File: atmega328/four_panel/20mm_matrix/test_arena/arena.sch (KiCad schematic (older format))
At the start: 29 parts, among them P1 CONN15, P10 CONN_2X2, P11 CONN_2X2, P12 CONN_2X2, P13 CONN_2X2, P14 CONN_2X2, P15 CONN_2X2, P16 CONN_2X2, P17 CONN_2X2, P18 CONN_2X2, P19 CONN_2X2, P2 CONN15, P20 CONN_2X2, P21 CONN_2X2, P22 CONN_20X2, P23 CONN_30X2, P24 CONN_2, P3 CONN15, P4 CONN15, P5 CONN15, P6 CONN15, P7 CONN_2X2, P8 CONN_2X2, P9 CONN_2X2

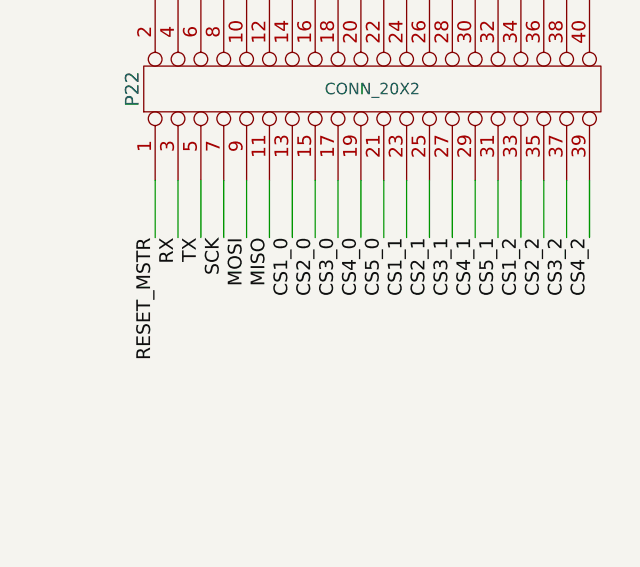
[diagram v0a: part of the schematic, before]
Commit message: Finished test arena for 4 x 20mm atmega328 panels.
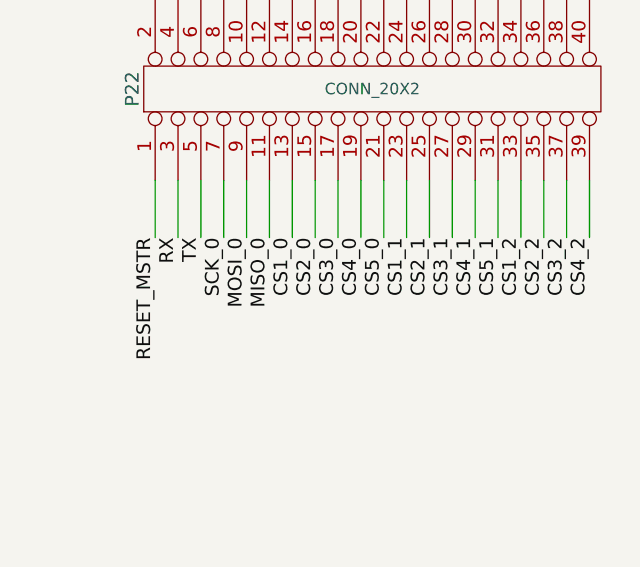
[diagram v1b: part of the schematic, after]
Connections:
- net MISO is gone; now on net MISO_0: P22.11 (P11)
- net MOSI is gone; now on net MOSI_0: P22.9 (P9)
- net SCK is gone; now on net SCK_0: P22.7 (P7)
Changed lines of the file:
@@
 LIBS:valves
 LIBS:conn15
+LIBS:arena-cache
 EELAYER 24 0
 EELAYER END
@@
 	2150 9700 2150 9850
 $Comp
-L +5V #PWR19
+L +5V #PWR01
 U 1 1 524B46C2
 P 2150 9300
-F 0 "#PWR19" H 2150 9390 20  0001 C CNN
+F 0 "#PWR01" H 2150 9390 20  0001 C CNN
 F 1 "+5V" H 2150 9390 30  0000 C CNN
 F 2 "" H 2150 9300 60  0000 C CNN
@@
 $EndComp
 $Comp
-L GND #PWR21
+L GND #PWR02
 U 1 1 524B46D1
 P 2150 9850
-F 0 "#PWR21" H 2150 9850 30  0001 C CNN
+F 0 "#PWR02" H 2150 9850 30  0001 C CNN
 F 1 "GND" H 2150 9780 30  0001 C CNN
 F 2 "" H 2150 9850 60  0000 C CNN
@@
 $EndComp
 $Comp
-L PWR_FLAG #FLG1
+L PWR_FLAG #FLG03
 U 1 1 524B46EA
 P 1250 9400
-F 0 "#FLG1" H 1250 9495 30  0001 C CNN
+F 0 "#FLG03" H 1250 9495 30  0001 C CNN
 F 1 "PWR_FLAG" H 1250 9580 30  0000 C CNN
 F 2 "" H 1250 9400 60  0000 C CNN
@@
 $EndComp
 $Comp
-L PWR_FLAG #FLG2
+L PWR_FLAG #FLG04
 U 1 1 524B46F9
 P 1650 9400
-F 0 "#FLG2" H 1650 9495 30  0001 C CNN
+F 0 "#FLG04" H 1650 9495 30  0001 C CNN
 F 1 "PWR_FLAG" H 1650 9580 30  0000 C CNN
 F 2 "" H 1650 9400 60  0000 C CNN
@@
 	1650 9400 1650 9850
 $Comp
-L GND #PWR20
+L GND #PWR05
 U 1 1 524B471D
 P 1650 9850
-F 0 "#PWR20" H 1650 9850 30  0001 C CNN
+F 0 "#PWR05" H 1650 9850 30  0001 C CNN
 F 1 "GND" H 1650 9780 30  0001 C CNN
 F 2 "" H 1650 9850 60  0000 C CNN
@@
 	900  9550 900  9300
 $Comp
-L +5V #PWR18
+L +5V #PWR06
 U 1 1 524B473D
 P 900 9300
-F 0 "#PWR18" H 900 9390 20  0001 C CNN
+F 0 "#PWR06" H 900 9390 20  0001 C CNN
 F 1 "+5V" H 900 9390 30  0000 C CNN
 F 2 "" H 900 9300 60  0000 C CNN
@@
 	850  1000 850  1200
 $Comp
-L +5V #PWR1
+L +5V #PWR07
 U 1 1 524B47C6
 P 850 1000
-F 0 "#PWR1" H 850 1090 20  0001 C CNN
+F 0 "#PWR07" H 850 1090 20  0001 C CNN
 F 1 "+5V" H 850 1090 30  0000 C CNN
 F 2 "" H 850 1000 60  0000 C CNN
@@
 	850  1300 850  1450
 $Comp
-L GND #PWR7
+L GND #PWR08
 U 1 1 524B47EA
 P 850 1450
-F 0 "#PWR7" H 850 1450 30  0001 C CNN
+F 0 "#PWR08" H 850 1450 30  0001 C CNN
 F 1 "GND" H 850 1380 30  0001 C CNN
 F 2 "" H 850 1450 60  0000 C CNN
@@
 	2600 1000 2600 1200
 $Comp
-L +5V #PWR2
+L +5V #PWR09
 U 1 1 524B4A08
 P 2600 1000
-F 0 "#PWR2" H 2600 1090 20  0001 C CNN
+F 0 "#PWR09" H 2600 1090 20  0001 C CNN
 F 1 "+5V" H 2600 1090 30  0000 C CNN
 F 2 "" H 2600 1000 60  0000 C CNN
@@
 	2600 1300 2600 1450
 $Comp
-L GND #PWR8
+L GND #PWR010
 U 1 1 524B4A10
 P 2600 1450
-F 0 "#PWR8" H 2600 1450 30  0001 C CNN
+F 0 "#PWR010" H 2600 1450 30  0001 C CNN
 F 1 "GND" H 2600 1380 30  0001 C CNN
 F 2 "" H 2600 1450 60  0000 C CNN
@@
 	4350 1000 4350 1200
 $Comp
-L +5V #PWR3
+L +5V #PWR011
 U 1 1 524B4A63
 P 4350 1000
-F 0 "#PWR3" H 4350 1090 20  0001 C CNN
+F 0 "#PWR011" H 4350 1090 20  0001 C CNN
 F 1 "+5V" H 4350 1090 30  0000 C CNN
 F 2 "" H 4350 1000 60  0000 C CNN
@@
 	4350 1300 4350 1450
 $Comp
-L GND #PWR9
+L GND #PWR012
 U 1 1 524B4A6B
 P 4350 1450
-F 0 "#PWR9" H 4350 1450 30  0001 C CNN
+F 0 "#PWR012" H 4350 1450 30  0001 C CNN
 F 1 "GND" H 4350 1380 30  0001 C CNN
 F 2 "" H 4350 1450 60  0000 C CNN
@@
 	6100 1000 6100 1200
 $Comp
-L +5V #PWR4
+L +5V #PWR013
 U 1 1 524B4A94
 P 6100 1000
-F 0 "#PWR4" H 6100 1090 20  0001 C CNN
+F 0 "#PWR013" H 6100 1090 20  0001 C CNN
 F 1 "+5V" H 6100 1090 30  0000 C CNN
 F 2 "" H 6100 1000 60  0000 C CNN
@@
 	6100 1300 6100 1450
 $Comp
-L GND #PWR10
+L GND #PWR014
 U 1 1 524B4A9C
 P 6100 1450
-F 0 "#PWR10" H 6100 1450 30  0001 C CNN
+F 0 "#PWR014" H 6100 1450 30  0001 C CNN
 F 1 "GND" H 6100 1380 30  0001 C CNN
 F 2 "" H 6100 1450 60  0000 C CNN
@@
 	7800 1000 7800 1200
 $Comp
-L +5V #PWR5
+L +5V #PWR015
 U 1 1 524B4AC7
 P 7800 1000
-F 0 "#PWR5" H 7800 1090 20  0001 C CNN
+F 0 "#PWR015" H 7800 1090 20  0001 C CNN
 F 1 "+5V" H 7800 1090 30  0000 C CNN
 F 2 "" H 7800 1000 60  0000 C CNN
@@
 	7800 1300 7800 1450
 $Comp
-L GND #PWR11
+L GND #PWR016
 U 1 1 524B4ACF
 P 7800 1450
-F 0 "#PWR11" H 7800 1450 30  0001 C CNN
+F 0 "#PWR016" H 7800 1450 30  0001 C CNN
 F 1 "GND" H 7800 1380 30  0001 C CNN
 F 2 "" H 7800 1450 60  0000 C CNN
@@
 	9450 1000 9450 1200
 $Comp
-L +5V #PWR6
+L +5V #PWR017
 U 1 1 524B5E35
 P 9450 1000
-F 0 "#PWR6" H 9450 1090 20  0001 C CNN
+F 0 "#PWR017" H 9450 1090 20  0001 C CNN
 F 1 "+5V" H 9450 1090 30  0000 C CNN
 F 2 "" H 9450 1000 60  0000 C CNN
@@
 	9450 1300 9450 1450
 $Comp
-L GND #PWR12
+L GND #PWR018
 U 1 1 524B5E3D
 P 9450 1450
-F 0 "#PWR12" H 9450 1450 30  0001 C CNN
+F 0 "#PWR018" H 9450 1450 30  0001 C CNN
 F 1 "GND" H 9450 1380 30  0001 C CNN
 F 2 "" H 9450 1450 60  0000 C CNN
@@
 Connection ~ 8500 7400
 $Comp
-L +5V #PWR14
+L +5V #PWR019
 U 1 1 524B6E04
 P 8500 5850
-F 0 "#PWR14" H 8500 5940 20  0001 C CNN
+F 0 "#PWR019" H 8500 5940 20  0001 C CNN
 F 1 "+5V" H 8500 5940 30  0000 C CNN
 F 2 "" H 8500 5850 60  0000 C CNN
@@
 $EndComp
 $Comp
-L GND #PWR16
+L GND #PWR020
 U 1 1 524B6E13
 P 8500 7650
-F 0 "#PWR16" H 8500 7650 30  0001 C CNN
+F 0 "#PWR020" H 8500 7650 30  0001 C CNN
 F 1 "GND" H 8500 7580 30  0001 C CNN
 F 2 "" H 8500 7650 60  0000 C CNN
@@
 	1550 7100 1550 7350
 Text Label 1350 7350 3    60   ~ 0
-SCK
+SCK_0
 Text Label 1450 7350 3    60   ~ 0
-MOSI
+MOSI_0
 Text Label 1550 7350 3    60   ~ 0
-MISO
+MISO_0
 Wire Wire Line
 	1650 7100 1650 7350
@@
 	3250 6150 3250 6350
 $Comp
-L +5V #PWR13
+L +5V #PWR021
 U 1 1 524B710E
 P 2850 5800
-F 0 "#PWR13" H 2850 5890 20  0001 C CNN
+F 0 "#PWR021" H 2850 5890 20  0001 C CNN
 F 1 "+5V" H 2850 5890 30  0000 C CNN
 F 2 "" H 2850 5800 60  0000 C CNN
@@
 $EndComp
 $Comp
-L GND #PWR15
+L GND #PWR022
 U 1 1 524B711D
 P 3250 6350
-F 0 "#PWR15" H 3250 6350 30  0001 C CNN
+F 0 "#PWR022" H 3250 6350 30  0001 C CNN
 F 1 "GND" H 3250 6280 30  0001 C CNN
 F 2 "" H 3250 6350 60  0000 C CNN
@@
 $EndComp
 $Comp
-L +5V #PWR17
+L +5V #PWR023
 U 1 1 524BBCA1
 P 5000 8950
-F 0 "#PWR17" H 5000 9040 20  0001 C CNN
+F 0 "#PWR023" H 5000 9040 20  0001 C CNN
 F 1 "+5V" H 5000 9040 30  0000 C CNN
 F 2 "" H 5000 8950 60  0000 C CNN
@@
 $EndComp
 $Comp
-L GND #PWR22
+L GND #PWR024
 U 1 1 524BBCDD
 P 5000 10150
-F 0 "#PWR22" H 5000 10150 30  0001 C CNN
+F 0 "#PWR024" H 5000 10150 30  0001 C CNN
 F 1 "GND" H 5000 10080 30  0001 C CNN
 F 2 "" H 5000 10150 60  0000 C CNN

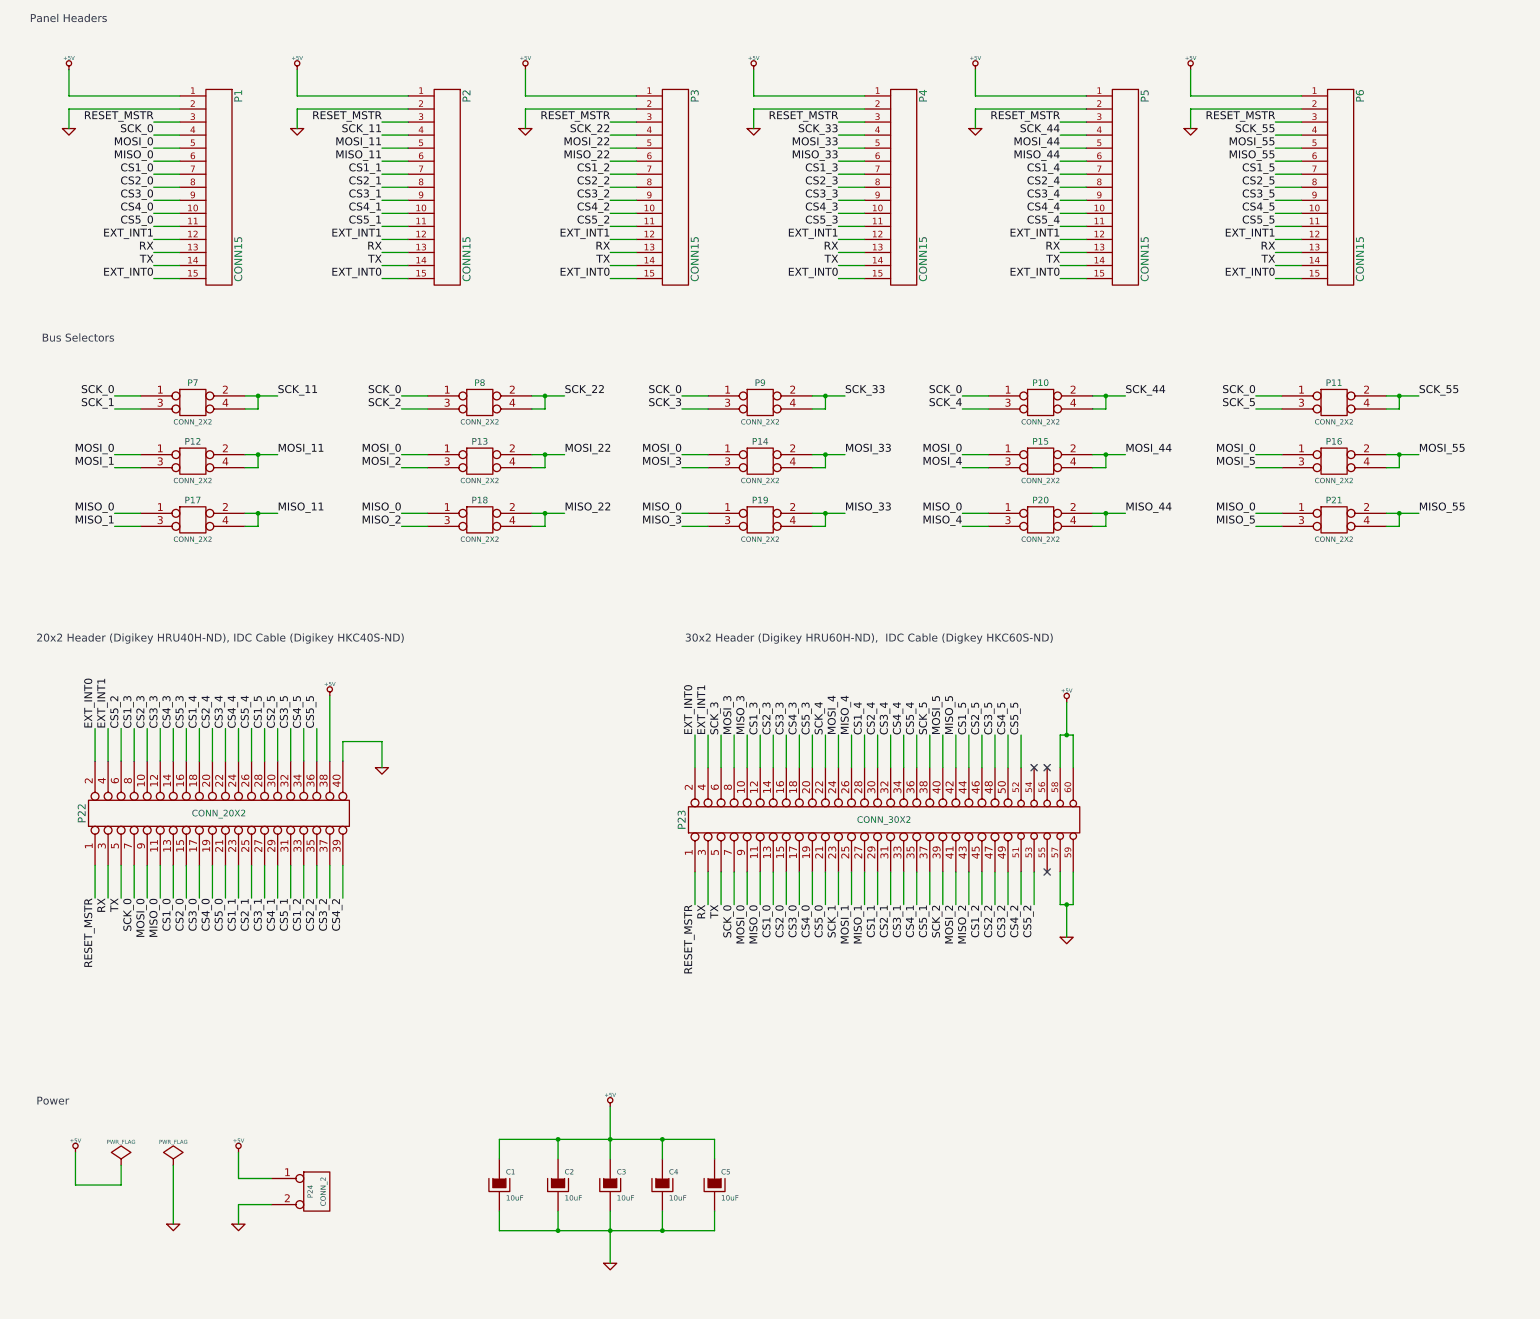
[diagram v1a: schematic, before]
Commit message: Finished 4x20mm matrix MAX6960 test arena.
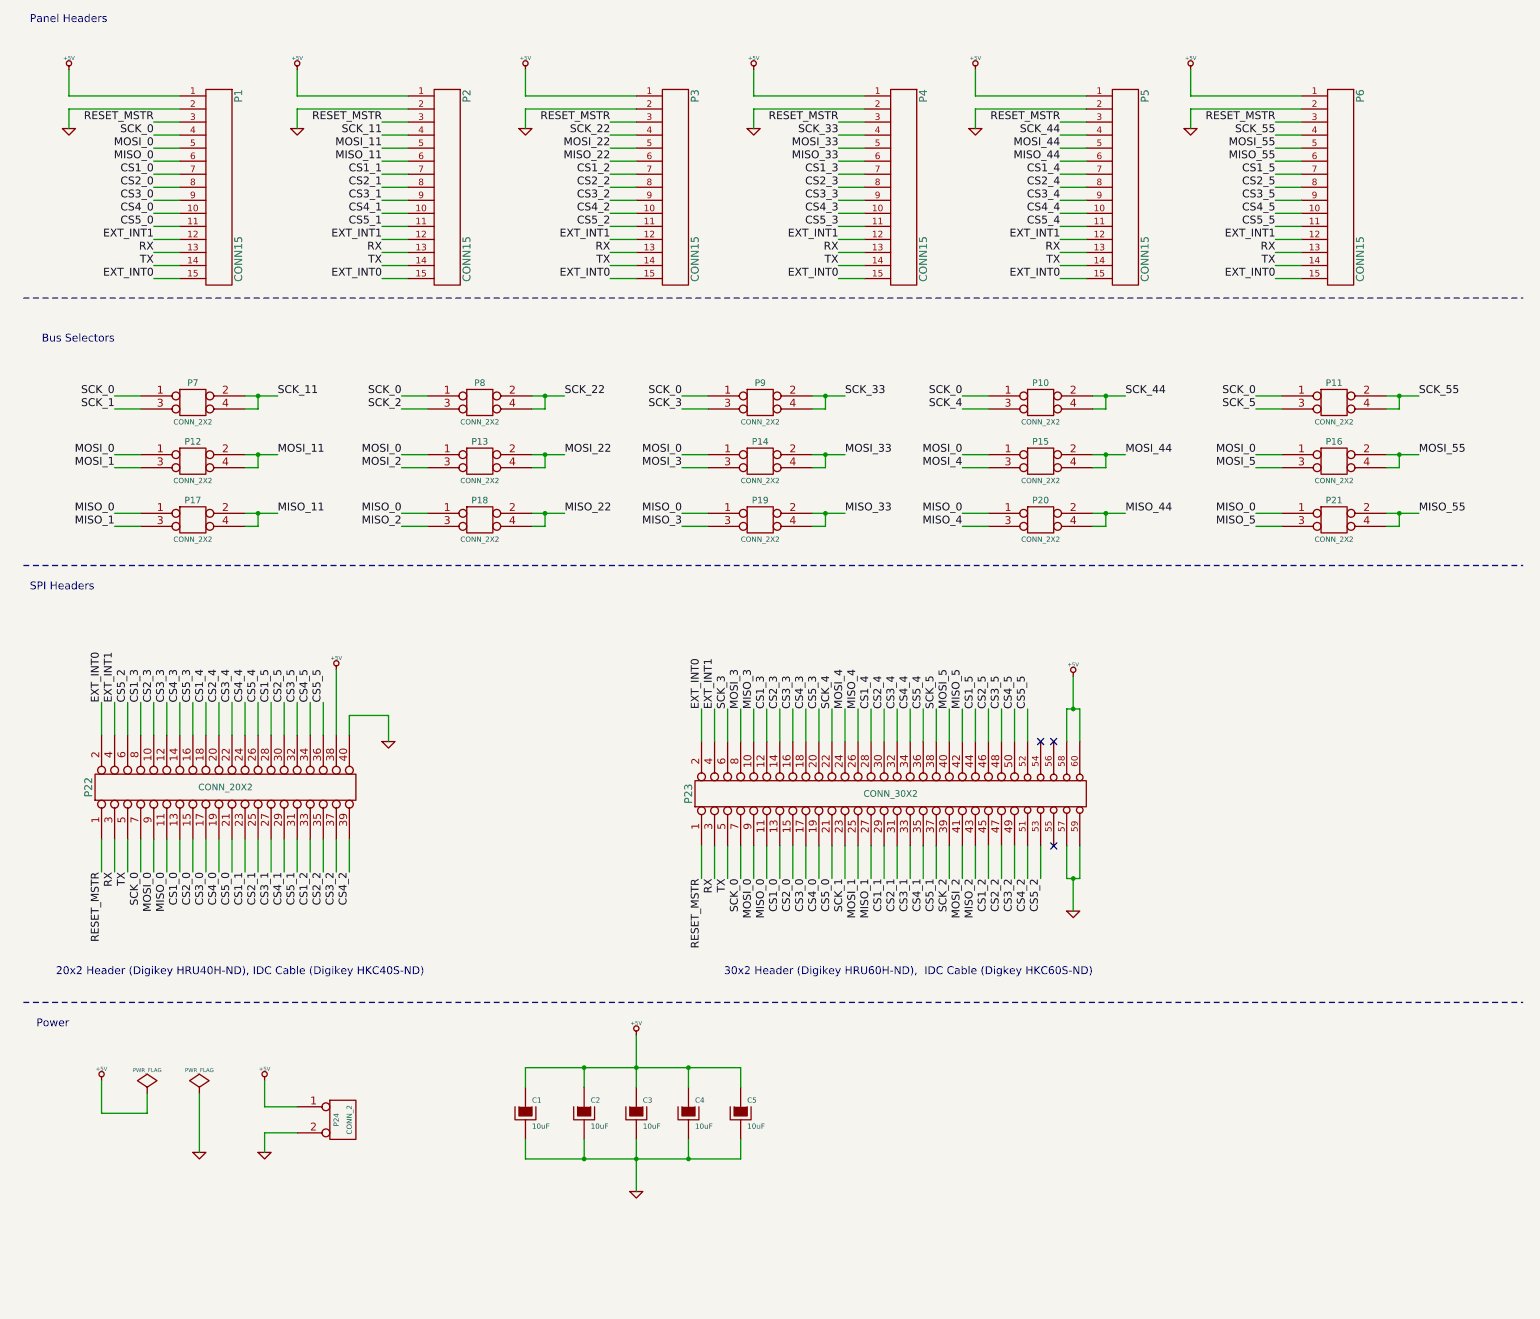
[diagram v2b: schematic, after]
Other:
- note added: "SPI Headers"
- moved on the sheet: C1, C2, C3, C4, C5, P22, P23, P24

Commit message: Added second communications header w/ common CS lines to  atmega328 4x20mm  test arena.
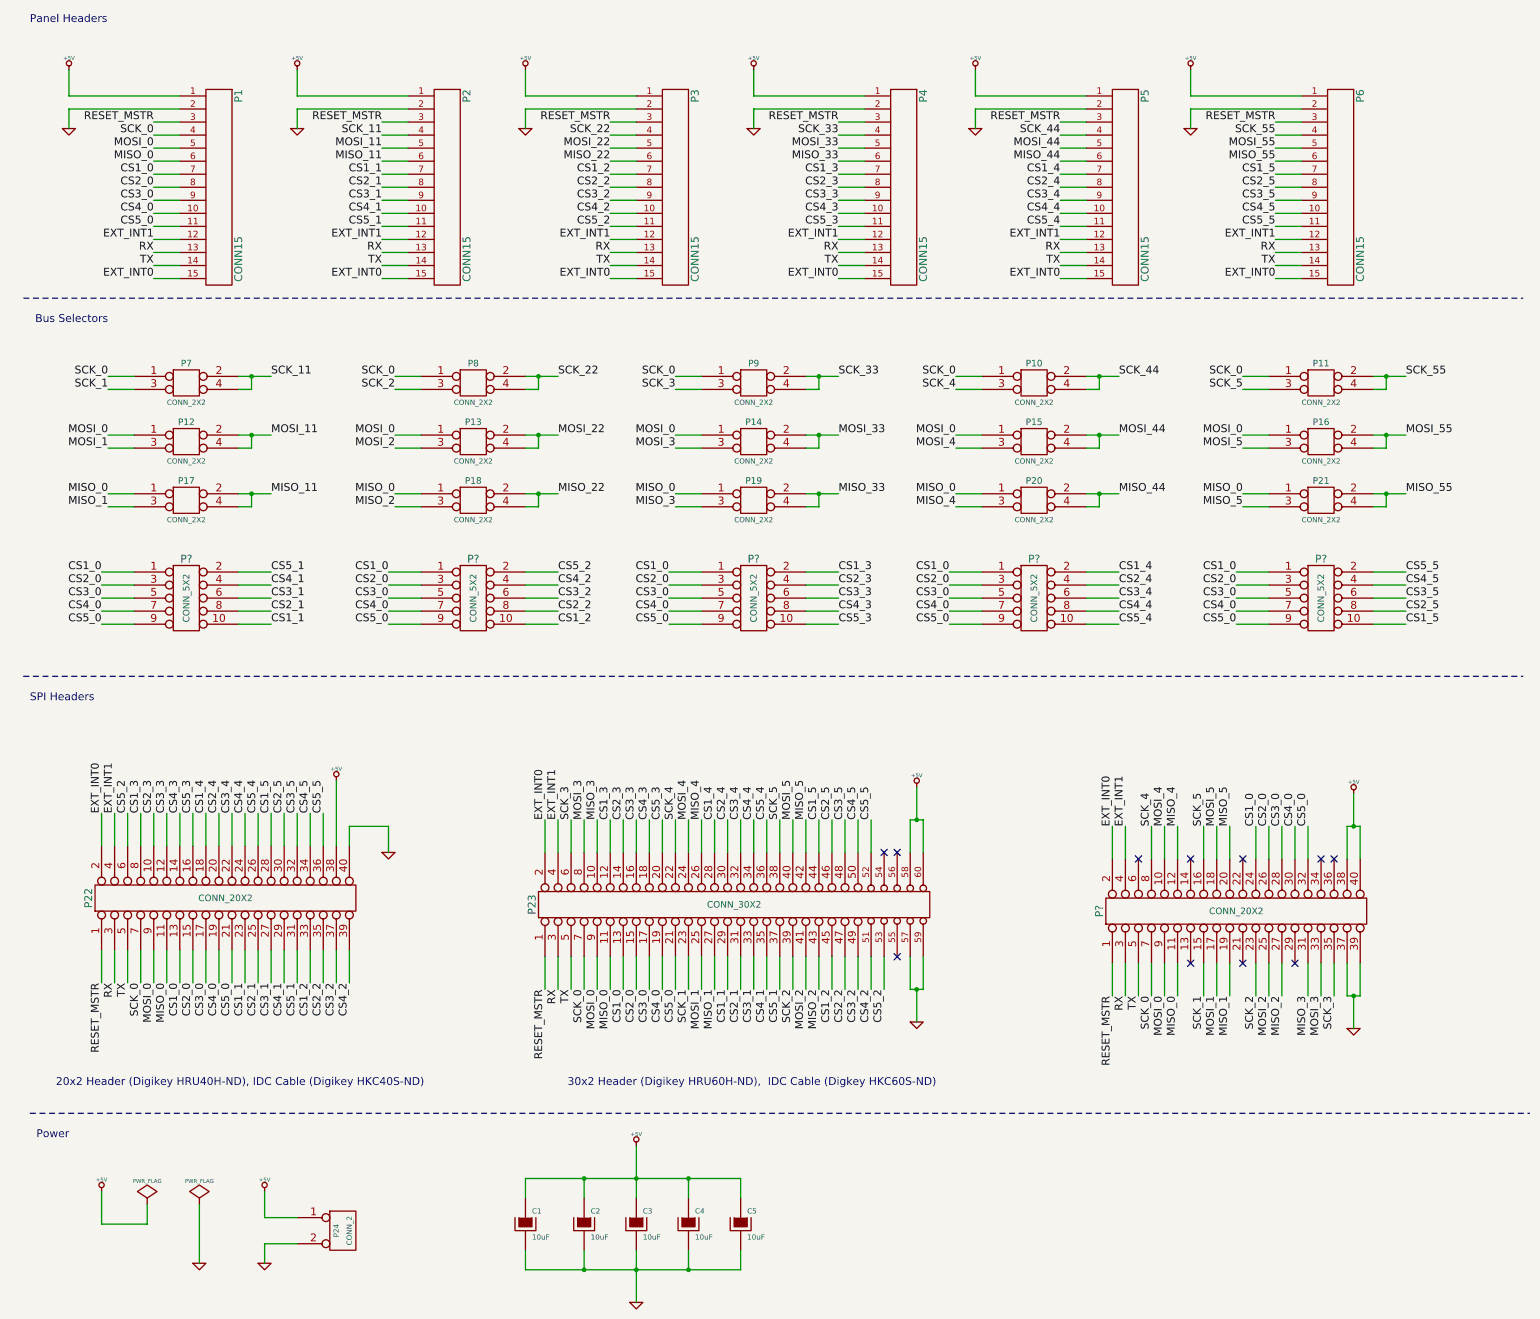
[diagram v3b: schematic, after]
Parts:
- added P?: CONN_20X2, symbol CONN_20X2
- added P? (x5): CONN_5X2, symbol CONN_5X2
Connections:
- net +5V: now also P?.38 (P38), P?.40 (P40)
- net CS1_0: now also P?.1, P?.1, P?.1, P?.1, P?.1, P?.24 (P24)
- net CS1_1: now also P?.10
- net CS1_2: now also P?.10
- net CS1_3: now also P?.2
- net CS1_4: now also P?.2
- net CS1_5: now also P?.10
- net CS2_0: now also P?.26 (P26), P?.3, P?.3, P?.3, P?.3, P?.3
- net CS2_1: now also P?.8
- net CS2_2: now also P?.8
- net CS2_3: now also P?.4
- net CS2_4: now also P?.4
- net CS2_5: now also P?.8
- net CS3_0: now also P?.28 (P28), P?.5, P?.5, P?.5, P?.5, P?.5
- net CS3_1: now also P?.6
- net CS3_2: now also P?.6
- net CS3_3: now also P?.6
- net CS3_4: now also P?.6
- net CS3_5: now also P?.6
- net CS4_0: now also P?.30 (P30), P?.7, P?.7, P?.7, P?.7, P?.7
- net CS4_1: now also P?.4
- net CS4_2: now also P?.4
- net CS4_3: now also P?.8
- net CS4_4: now also P?.8
- net CS4_5: now also P?.4
- net CS5_0: now also P?.32 (P32), P?.9, P?.9, P?.9, P?.9, P?.9
- net CS5_1: now also P?.2
- net CS5_2: now also P?.2
- net CS5_3: now also P?.10
- net CS5_4: now also P?.10
- net CS5_5: now also P?.2
- net EXT_INT0: now also P?.2 (P2)
- net EXT_INT1: now also P?.4 (P4)
- net GND: now also P?.37 (P37), P?.39 (P39)
- net MISO_0: now also P?.11 (P11)
- net MISO_1: now also P?.19 (P19)
- net MISO_2: now also P?.27 (P27)
- net MISO_3: now also P?.31 (P31)
- net MISO_4: now also P?.12 (P12)
- net MISO_5: now also P?.20 (P20)
- net MOSI_0: now also P?.9 (P9)
- net MOSI_1: now also P?.17 (P17)
- net MOSI_2: now also P?.25
- net MOSI_3: now also P?.33 (P33)
- net MOSI_4: now also P?.10 (P10)
- net MOSI_5: now also P?.18 (P18)
- net RESET_MSTR: now also P?.1 (P1)
- net RX: now also P?.3 (P3)
- net SCK_0: now also P?.7 (P7)
- net SCK_1: now also P?.15 (P15)
- net SCK_2: now also P?.23 (P23)
- net SCK_3: now also P?.35 (P35)
- net SCK_4: now also P?.8 (P8)
- net SCK_5: now also P?.16 (P16)
- net TX: now also P?.5 (P5)
- no-connect marks 3 -> 11
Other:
- moved on the sheet: C1, C2, C3, C4, C5, P10, P11, P12, P13, P14, P15, P16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
